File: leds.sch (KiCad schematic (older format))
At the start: 218 parts, among them U10 TLC5955, U11 TLC5955, U12 TLC5955, U13 TLC5955, U14 TLC5955, U15 TLC5955, U4 TLC5955, U5 TLC5955, U6 TLC5955, U7 TLC5955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

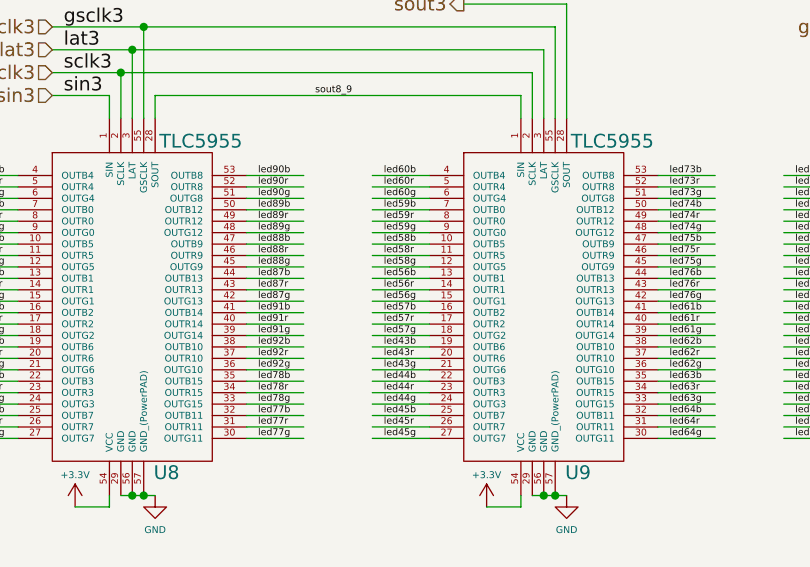
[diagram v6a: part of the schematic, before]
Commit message: Cleanup back routing on U9
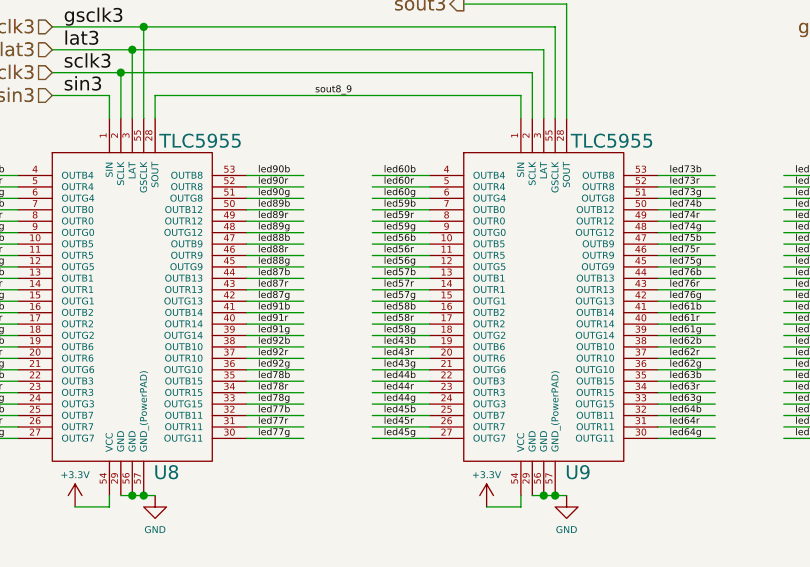
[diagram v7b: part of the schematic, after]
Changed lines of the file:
@@
 led55g
+Wire Wire Line
+	10700 2200 10450 2200
+Wire Wire Line
+	10700 2250 10450 2250
+Wire Wire Line
+	7100 3050 6850 3050
+Text Label 10500 2200 0    30   ~ 0
+led56b
+Text Label 10500 2250 0    30   ~ 0
+led56r
+Text Label 10500 2300 0    30   ~ 0
+led56g
 Wire Wire Line
 	10700 2350 10450 2350
@@
 	10700 2400 10450 2400
 Wire Wire Line
-	7100 3050 6850 3050
+	4750 2300 4500 2300
 Text Label 10500 2350 0    30   ~ 0
-led56b
+led57b
 Text Label 10500 2400 0    30   ~ 0
-led56r
+led57r
 Text Label 10500 2450 0    30   ~ 0
-led56g
+led57g
 Wire Wire Line
 	10700 2500 10450 2500
@@
 	10700 2550 10450 2550
 Wire Wire Line
-	4750 2300 4500 2300
+	8350 2150 8100 2150
 Text Label 10500 2500 0    30   ~ 0
-led57b
+led58b
 Text Label 10500 2550 0    30   ~ 0
-led57r
+led58r
 Text Label 10500 2600 0    30   ~ 0
-led57g
-Wire Wire Line
-	10700 2200 10450 2200
-Wire Wire Line
-	10700 2250 10450 2250
-Wire Wire Line
-	8350 2150 8100 2150
-Text Label 10500 2200 0    30   ~ 0
-led58b
-Text Label 10500 2250 0    30   ~ 0
-led58r
-Text Label 10500 2300 0    30   ~ 0
 led58g
 Wire Wire Line

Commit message: Some misc. small LED routing cleanups.
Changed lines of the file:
@@
 led79g
 Wire Wire Line
-	2950 2650 2700 2650
-Wire Wire Line
-	2950 2700 2700 2700
+	2950 2800 2700 2800
+Wire Wire Line
+	2950 2850 2700 2850
 Wire Wire Line
 	10150 3050 9900 3050
-Text Label 2750 2650 0    30   ~ 0
+Text Label 2750 2800 0    30   ~ 0
 led80b
-Text Label 2750 2700 0    30   ~ 0
+Text Label 2750 2850 0    30   ~ 0
 led80r
-Text Label 2750 2750 0    30   ~ 0
+Text Label 2750 2900 0    30   ~ 0
 led80g
 Wire Wire Line
@@
 led92g
 Wire Wire Line
-	2950 2800 2700 2800
-Wire Wire Line
-	2950 2850 2700 2850
+	2950 2650 2700 2650
+Wire Wire Line
+	2950 2700 2700 2700
 Wire Wire Line
 	11950 2000 11700 2000
-Text Label 2750 2800 0    30   ~ 0
+Text Label 2750 2650 0    30   ~ 0
 led93b
-Text Label 2750 2850 0    30   ~ 0
+Text Label 2750 2700 0    30   ~ 0
 led93r
-Text Label 2750 2900 0    30   ~ 0
+Text Label 2750 2750 0    30   ~ 0
 led93g
 Wire Wire Line
@@
 $EndComp
 Wire Wire Line
-	12500 7800 12250 7800
-Wire Wire Line
-	12500 7850 12250 7850
+	12500 7650 12250 7650
+Wire Wire Line
+	12500 7700 12250 7700
 Wire Wire Line
 	12500 7900 12250 7900
-Text Label 12300 7800 0    30   ~ 0
+Text Label 12300 7650 0    30   ~ 0
 led107b
-Text Label 12300 7850 0    30   ~ 0
+Text Label 12300 7700 0    30   ~ 0
 led107r
-Text Label 12300 7900 0    30   ~ 0
+Text Label 12300 7750 0    30   ~ 0
 led107g
 Wire Wire Line
@@
 led121g
 Wire Wire Line
-	12500 7650 12250 7650
-Wire Wire Line
-	12500 7700 12250 7700
+	12500 7800 12250 7800
+Wire Wire Line
+	12500 7850 12250 7850
 Wire Wire Line
 	12500 7450 12250 7450
-Text Label 12300 7650 0    30   ~ 0
+Text Label 12300 7800 0    30   ~ 0
 led122b
-Text Label 12300 7700 0    30   ~ 0
+Text Label 12300 7850 0    30   ~ 0
 led122r
-Text Label 12300 7750 0    30   ~ 0
+Text Label 12300 7900 0    30   ~ 0
 led122g
 Wire Wire Line
